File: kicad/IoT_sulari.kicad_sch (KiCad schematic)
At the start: 37 parts, among them J1 73412-0110, J2 73412-0110, J3 20021121-00010C4LF, J4 20021121-00010C4LF, J6 20021121-00010C4LF, SW1 SW_SPST, SW2 TL3301DF160QG, SW3 TL3301DF160QG, SW4 TL3301DF160QG, SW5 TL3301DF160QG, U2 NRF9160

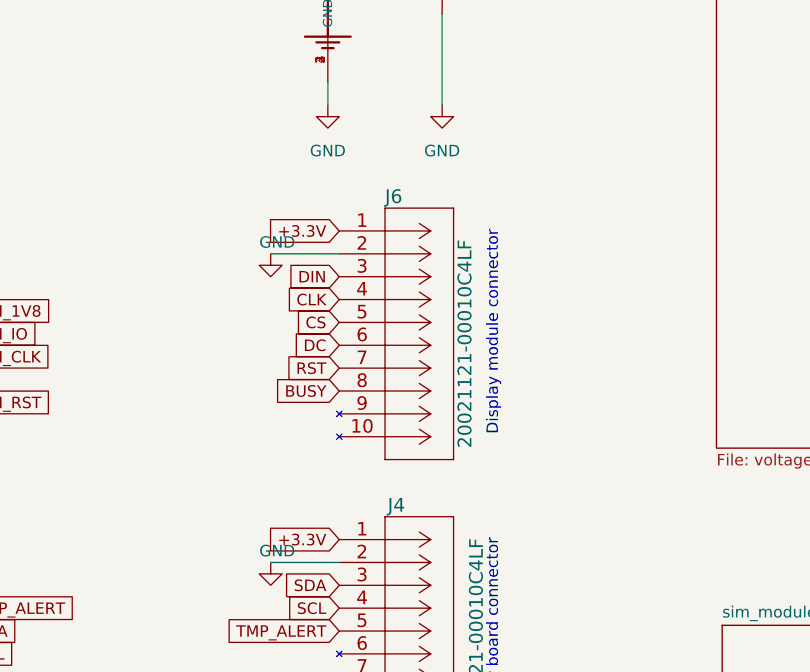
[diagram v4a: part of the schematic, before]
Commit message: sensorboard modify and mainboard connector add
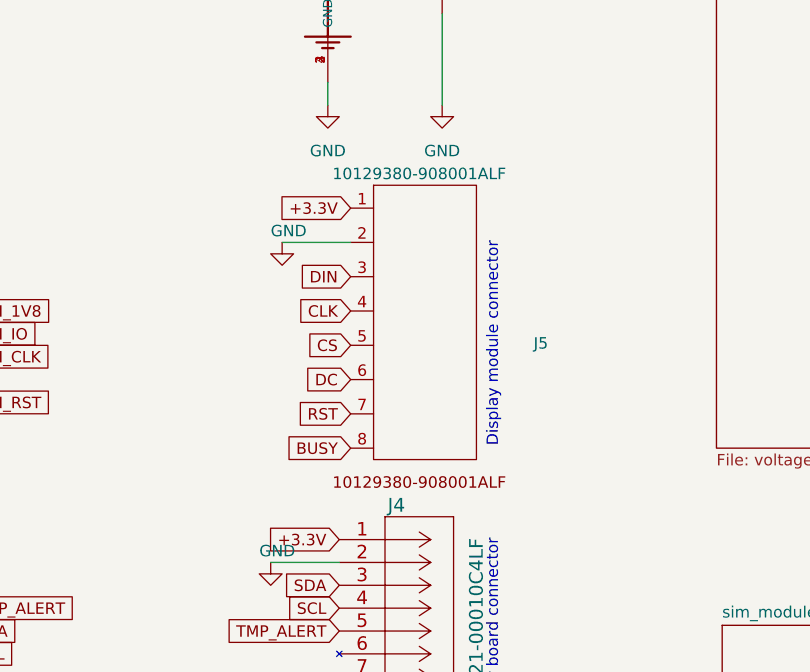
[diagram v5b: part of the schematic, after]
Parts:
- removed J6: 20021121-00010C4LF, 20021121-00010C4LF:20021121-00010C4LF, symbol 20021121-00010C4LF:20021121-00010C4LF
- added J5: 10129380-908001ALF, 10129380-908001ALF:10129380-908001ALF, symbol 10129380-908001ALF:10129380-908001ALF
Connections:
- net +3.3V: now also J5.1
- net BUSY: now also J5.8
- net CLK: now also J5.4
- net CS: now also J5.5
- net DC: now also J5.6
- net DIN: now also J5.3
- net GND: now also J5.2
- net RST: now also J5.7
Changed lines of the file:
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@@
     (stroke (width 0) (type default))
   )
-  (wire (pts (xy 256.54 67.31) (xy 264.16 67.31))
+  (wire (pts (xy 257.81 66.04) (xy 265.43 66.04))
     (stroke (width 0) (type default))
   )
@@
     (effects (font (size 1.27 1.27)) (justify right bottom))
   )
-  (text "Display module connector" (at 281.94 64.77 90)
+  (text "Display module connector" (at 281.94 66.04 90)
     (effects (font (size 1.27 1.27)) (justify right bottom))
   )
@@
     (effects (font (size 1.27 1.27)) (justify left bottom))
   )
-  (global_label "DC" (shape input) (at 264.16 77.47 180) (fields_autoplaced)
-    (effects (font (size 1.27 1.27)) (justify right))
-    (property "Intersheetrefs" "${INTERSHEET_REFS}" (at 258.7142 77.47 0)
+  (global_label "DC" (shape input) (at 265.43 81.28 180) (fields_autoplaced)
+    (effects (font (size 1.27 1.27)) (justify right))
+    (property "Intersheetrefs" "${INTERSHEET_REFS}" (at 259.9842 81.28 0)
       (effects (font (size 1.27 1.27)) (justify right) hide)
     )
@@
     )
   )
-  (global_label "CLK" (shape input) (at 264.16 72.39 180) (fields_autoplaced)
-    (effects (font (size 1.27 1.27)) (justify right))
-    (property "Intersheetrefs" "${INTERSHEET_REFS}" (at 257.6861 72.39 0)
+  (global_label "CLK" (shape input) (at 265.43 73.66 180) (fields_autoplaced)
+    (effects (font (size 1.27 1.27)) (justify right))
+    (property "Intersheetrefs" "${INTERSHEET_REFS}" (at 258.9561 73.66 0)
       (effects (font (size 1.27 1.27)) (justify right) hide)
     )
@@
     )
   )
-  (global_label "RST" (shape input) (at 264.16 80.01 180) (fields_autoplaced)
-    (effects (font (size 1.27 1.27)) (justify right))
-    (property "Intersheetrefs" "${INTERSHEET_REFS}" (at 257.8071 80.01 0)
+  (global_label "RST" (shape input) (at 265.43 85.09 180) (fields_autoplaced)
+    (effects (font (size 1.27 1.27)) (justify right))
+    (property "Intersheetrefs" "${INTERSHEET_REFS}" (at 259.0771 85.09 0)
       (effects (font (size 1.27 1.27)) (justify right) hide)
     )
@@
     )
   )
-  (global_label "+3.3V" (shape input) (at 264.16 64.77 180) (fields_autoplaced)
-    (effects (font (size 1.27 1.27)) (justify right))
-    (property "Intersheetrefs" "${INTERSHEET_REFS}" (at 255.5694 64.77 0)
+  (global_label "+3.3V" (shape input) (at 265.43 62.23 180) (fields_autoplaced)
+    (effects (font (size 1.27 1.27)) (justify right))
+    (property "Intersheetrefs" "${INTERSHEET_REFS}" (at 256.8394 62.23 0)
       (effects (font (size 1.27 1.27)) (justify right) hide)
     )
@@
     )
   )
-  (global_label "CS" (shape input) (at 264.16 74.93 180) (fields_autoplaced)
-    (effects (font (size 1.27 1.27)) (justify right))
-    (property "Intersheetrefs" "${INTERSHEET_REFS}" (at 258.7747 74.93 0)
+  (global_label "CS" (shape input) (at 265.43 77.47 180) (fields_autoplaced)
+    (effects (font (size 1.27 1.27)) (justify right))
+    (property "Intersheetrefs" "${INTERSHEET_REFS}" (at 260.0447 77.47 0)
       (effects (font (size 1.27 1.27)) (justify right) hide)
     )
@@
     )
   )
-  (global_label "BUSY" (shape input) (at 264.16 82.55 180) (fields_autoplaced)
-    (effects (font (size 1.27 1.27)) (justify right))
-    (property "Intersheetrefs" "${INTERSHEET_REFS}" (at 256.3556 82.55 0)
+  (global_label "BUSY" (shape input) (at 265.43 88.9 180) (fields_autoplaced)
+    (effects (font (size 1.27 1.27)) (justify right))
+    (property "Intersheetrefs" "${INTERSHEET_REFS}" (at 257.6256 88.9 0)
       (effects (font (size 1.27 1.27)) (justify right) hide)
     )
@@
     )
   )
-  (global_label "DIN" (shape input) (at 264.16 69.85 180) (fields_autoplaced)
-    (effects (font (size 1.27 1.27)) (justify right))
-    (property "Intersheetrefs" "${INTERSHEET_REFS}" (at 258.0489 69.85 0)
+  (global_label "DIN" (shape input) (at 265.43 69.85 180) (fields_autoplaced)
+    (effects (font (size 1.27 1.27)) (justify right))
+    (property "Intersheetrefs" "${INTERSHEET_REFS}" (at 259.3189 69.85 0)
       (effects (font (size 1.27 1.27)) (justify right) hide)
     )
@@
     )
   )
+  (symbol (lib_id "10129380-908001ALF:10129380-908001ALF") (at 273.05 74.93 0) (unit 1)
+    (in_bom yes) (on_board yes) (dnp no) (fields_autoplaced)
+    (property "Reference" "J5" (at 285.75 77.2517 0)
+      (effects (font (size 1.27 1.27)) (justify left))
+    )
+    (property "Value" "10129380-908001ALF" (at 273.05 58.42 0)
+      (effects (font (size 1.27 1.27)))
+    )
+    (property "Footprint" "10129380-908001ALF:10129380-908001ALF" (at 273.05 58.42 0)
+      (effects (font (size 1.27 1.27)) hide)
+    )
+    (property "Datasheet" "" (at 273.05 58.42 0)
+      (effects (font (size 1.27 1.27)) hide)
+    )
+    (property "Digikey" "10129380-908001ALF-ND" (at 273.05 74.93 0)
+      (effects (font (size 1.27 1.27)) hide)
+    )
+    (pin "1")
+    (pin "2")
+    (pin "3")
+    (pin "4")
+    (pin "5")
+    (pin "6")
+    (pin "7")
+    (pin "8")
+    (instances
+      (project "IoT_sulari"
+        (path "/184b47ed-2c2b-4c02-be35-d18f4f4e5685"
+          (reference "J5") (unit 1)
+        )
+      )
+    )
+  )
   (symbol (lib_id "power:GND") (at 19.05 176.53 0) (unit 1)
     (in_bom yes) (on_board yes) (dnp no) (fields_autoplaced)
@@
     )
   )
-  (symbol (lib_name "20021121-00010C4LF_1") (lib_id "20021121-00010C4LF:20021121-00010C4LF") (at 264.16 64.77 0) (unit 1)
-    (in_bom yes) (on_board yes) (dnp no)
-    (property "Reference" "J6" (at 269.24 60.96 0)
-      (effects (font (size 1.524 1.524)) (justify left))
-    )
-    (property "Value" "20021121-00010C4LF" (at 278.13 88.9 90)
-      (effects (font (size 1.524 1.524)) (justify left))
-    )
-    (property "Footprint" "20021121-00010C4LF:20021121-00010C4LF" (at 274.32 76.454 0)
-      (effects (font (size 1.524 1.524)) hide)
-    )
-    (property "Datasheet" "" (at 264.16 64.77 0)
-      (effects (font (size 1.524 1.524)))
-    )
-    (property "Digikey" "609-3695-1-ND" (at 264.16 64.77 0)
-      (effects (font (size 1.27 1.27)) hide)
-    )
-    (pin "1")
-    (pin "10")
-    (pin "2")
-    (pin "3")
-    (pin "4")
-    (pin "5")
-    (pin "6")
-    (pin "7")
-    (pin "8")
-    (pin "9")
-    (instances
-      (project "IoT_sulari"
-        (path "/184b47ed-2c2b-4c02-be35-d18f4f4e5685"
-          (reference "J6") (unit 1)
-        )
-      )
-    )
-  )
   (symbol (lib_id "Device:R") (at 181.61 149.86 0) (unit 1)
     (in_bom yes) (on_board yes) (dnp no)
@@
     )
   )
-  (symbol (lib_id "power:GND") (at 256.54 67.31 0) (unit 1)
+  (symbol (lib_id "power:GND") (at 257.81 66.04 0) (unit 1)
     (in_bom yes) (on_board yes) (dnp no)
-    (property "Reference" "#PWR030" (at 256.54 73.66 0)
-      (effects (font (size 1.27 1.27)) hide)
-    )
-    (property "Value" "GND" (at 255.27 66.04 0)
+    (property "Reference" "#PWR030" (at 257.81 72.39 0)
+      (effects (font (size 1.27 1.27)) hide)
+    )
+    (property "Value" "GND" (at 256.54 64.77 0)
       (effects (font (size 1.27 1.27)) (justify left))
     )
-    (property "Footprint" "" (at 256.54 67.31 0)
-      (effects (font (size 1.27 1.27)) hide)
-    )
-    (property "Datasheet" "" (at 256.54 67.31 0)
-      (effects (font (size 1.27 1.27)) hide)
-    )
+    (property "Footprint" "" (at 257.81 66.04 0)
+      (effects (font (size 1.27 1.27)) hide)
+    )
+    (property "Datasheet" "" (at 257.81 66.04 0)
+      (effects (font (size 1.27 1.27)) hide)
+    )

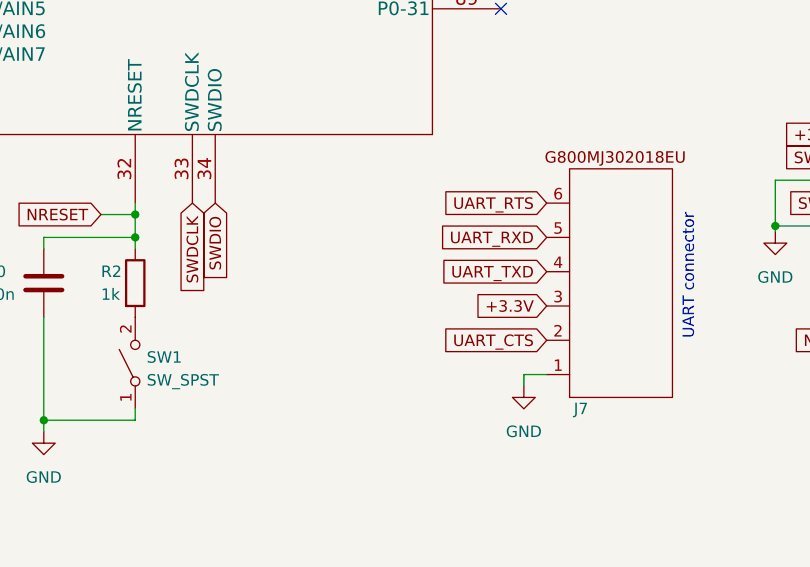
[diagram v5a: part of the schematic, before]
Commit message: changed Display connector
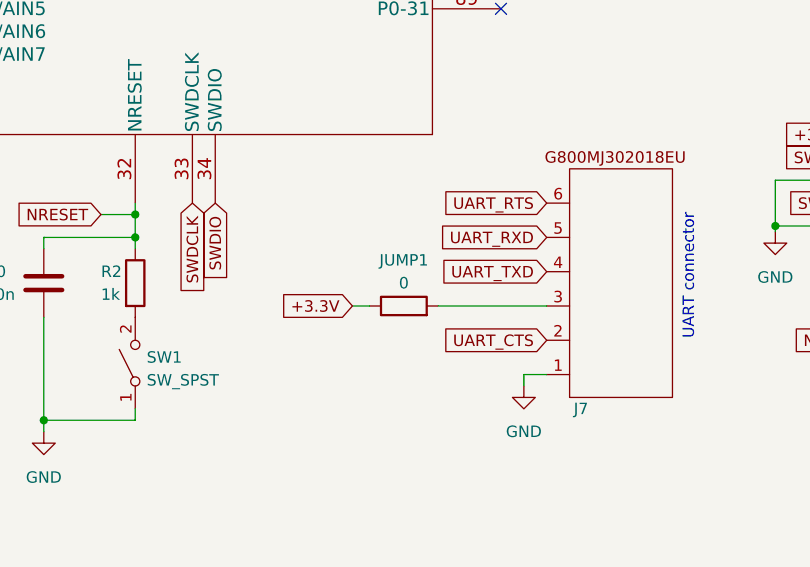
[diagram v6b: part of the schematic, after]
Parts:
- added JUMP1: 0, Resistor_SMD:R_0805_2012Metric_Pad1.20x1.40mm_HandSolder, symbol Device:R
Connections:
- net +3.3V: now also JUMP1.1; no longer J7.3
- new net: J7.3, JUMP1.2
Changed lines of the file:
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@@
+    (stroke (width 0) (type default))
+  )
+  (wire (pts (xy 205.74 152.4) (xy 207.645 152.4))
     (stroke (width 0) (type default))
   )
@@
   )
   (wire (pts (xy 106.68 149.86) (xy 106.68 152.4))
+    (stroke (width 0) (type default))
+  )
+  (wire (pts (xy 215.265 152.4) (xy 227.33 152.4))
     (stroke (width 0) (type default))
   )
@@
     )
   )
-  (global_label "+3.3V" (shape input) (at 227.33 152.4 180) (fields_autoplaced)
-    (effects (font (size 1.27 1.27)) (justify right))
-    (property "Intersheetrefs" "${INTERSHEET_REFS}" (at 218.7394 152.4 0)
+  (global_label "+3.3V" (shape input) (at 205.74 152.4 180) (fields_autoplaced)
+    (effects (font (size 1.27 1.27)) (justify right))
+    (property "Intersheetrefs" "${INTERSHEET_REFS}" (at 197.1494 152.4 0)
       (effects (font (size 1.27 1.27)) (justify right) hide)
     )
@@
         )
       )
+    )
+  )
+  (symbol (lib_id "Device:R") (at 211.455 152.4 90) (unit 1)
+    (in_bom yes) (on_board yes) (dnp no) (fields_autoplaced)
+    (property "Reference" "JUMP1" (at 211.455 147.32 90)
+      (effects (font (size 1.27 1.27)))
+    )
+    (property "Value" "0" (at 211.455 149.86 90)
+      (effects (font (size 1.27 1.27)))
+    )
+    (property "Footprint" "Resistor_SMD:R_0805_2012Metric_Pad1.20x1.40mm_HandSolder" (at 211.455 154.178 90)
+      (effects (font (size 1.27 1.27)) hide)
+    )
+    (property "Datasheet" "~" (at 211.455 152.4 0)
+      (effects (font (size 1.27 1.27)) hide)
+    )
+    (pin "1")
+    (pin "2")
+    (instances
+      (project "IoT_sulari"
+        (path "/184b47ed-2c2b-4c02-be35-d18f4f4e5685"
+          (reference "JUMP1") (unit 1)
+        )
+      )
